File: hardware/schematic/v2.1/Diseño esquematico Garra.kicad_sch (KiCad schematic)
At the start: 20 parts

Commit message: fix: PDF
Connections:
- net SW renamed Stick_ON
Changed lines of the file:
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@@
 		)
 	)
-	(global_label "SW"
+	(global_label "Stick_ON"
 		(shape input)
 		(at 182.88 133.35 180)
@@
 		)
 	)
-	(global_label "SW"
+	(global_label "Stick_ON"
 		(shape input)
 		(at 269.24 143.51 0)

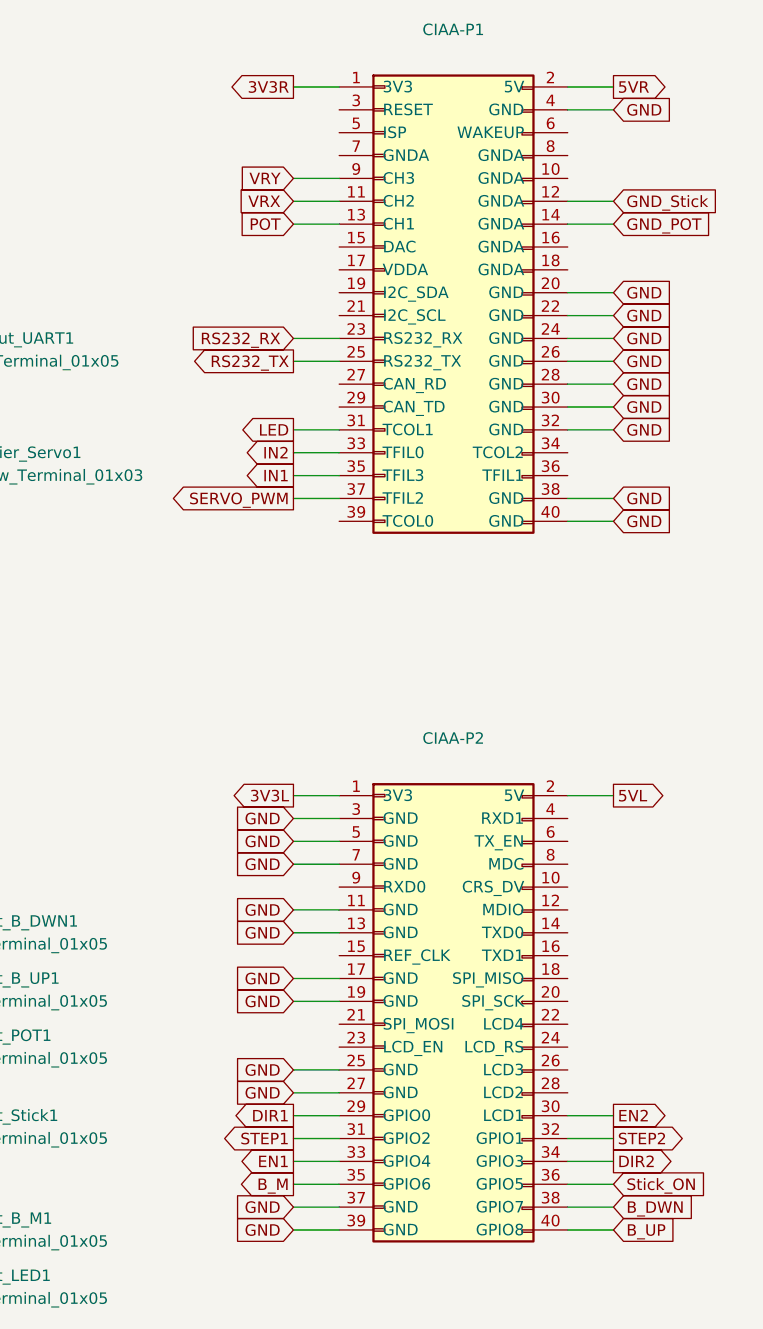
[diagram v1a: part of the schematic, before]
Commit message: Pcb branch (#8)
* refactor

* feat: PCB routing first stage completed

* docs: Schematics PDF added

* fix: PCB border colision

* feat: Copper layers added to the PCB

* feat: New PCB design with new components [LED, B_M]

* feat: add through holes for connectivity & GNDs links

* feat: hole diameter adjustment

* fix: PDF

* feat: change route system in PCB

---------

Co-authored-by: ManuSavenia <saveniamanuel@egmail.com>
Co-authored-by: Iván Valentín Polanis <polanis.ivan@alu.ing.unlp.edu.ar>
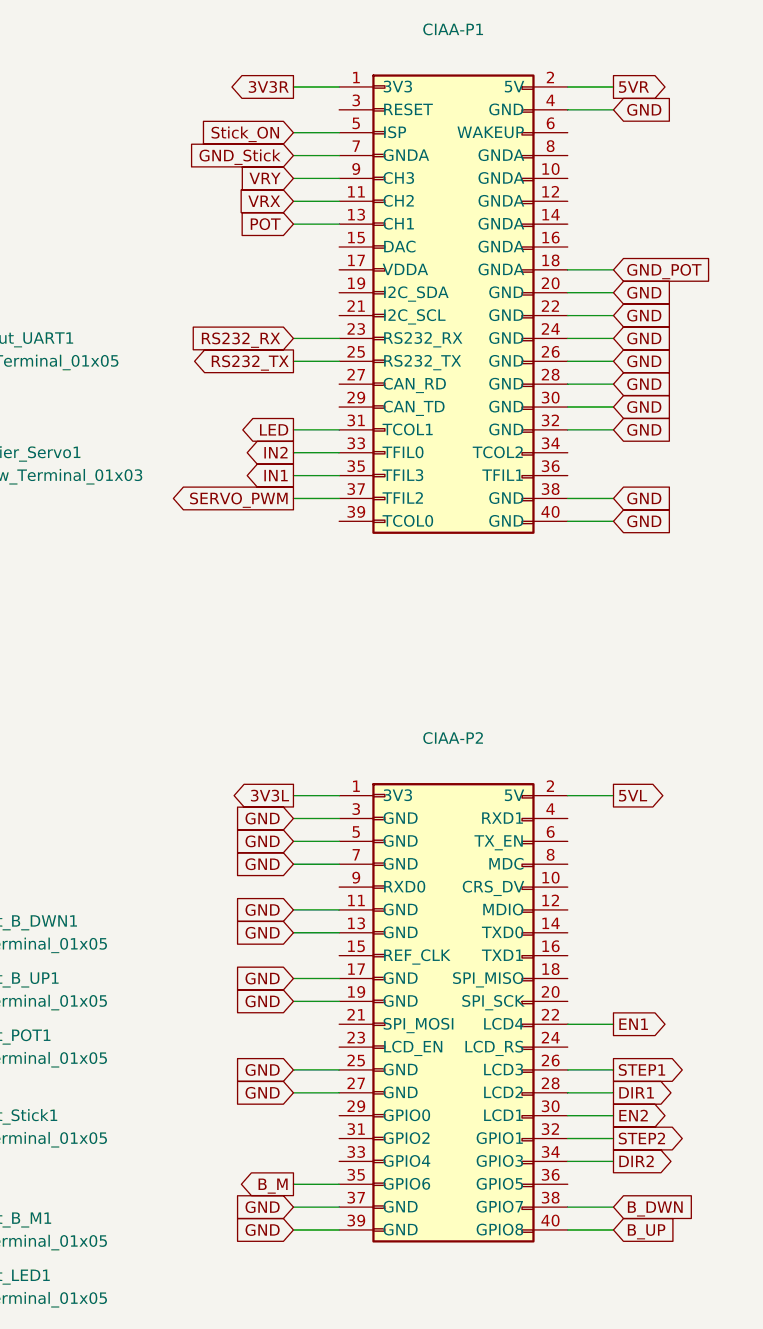
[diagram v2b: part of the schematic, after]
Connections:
- net DIR1: now also CIAA-P2.28 (LCD2); no longer CIAA-P2.29 (GPIO0)
- net EN1: now also CIAA-P2.22 (LCD4); no longer CIAA-P2.33 (GPIO4)
- net GND_POT: now also CIAA-P1.18 (GNDA); no longer CIAA-P1.14 (GNDA)
- net GND_Stick: now also CIAA-P1.7 (GNDA); no longer CIAA-P1.12 (GNDA)
- net STEP1: now also CIAA-P2.26 (LCD3); no longer CIAA-P2.31 (GPIO2)
- net Stick_ON: now also CIAA-P1.5 (ISP); no longer CIAA-P2.36 (GPIO5)
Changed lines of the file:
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@@
-	(wire
-		(pts
-			(xy 269.24 34.29) (xy 264.16 34.29)
-		)
-		(stroke
-			(width 0)
-			(type default)
-		)
-	)
 	(wire
 		(pts
@@
 	(wire
 		(pts
+			(xy 264.16 133.35) (xy 269.24 133.35)
+		)
+		(stroke
+			(width 0)
+			(type default)
+		)
+	)
+	(wire
+		(pts
 			(xy 189.23 85.09) (xy 189.23 86.36)
 		)
@@
 	(wire
 		(pts
-			(xy 233.68 135.89) (xy 238.76 135.89)
-		)
-		(stroke
-			(width 0)
-			(type default)
-		)
-	)
-	(wire
-		(pts
 			(xy 182.88 143.51) (xy 187.96 143.51)
 		)
@@
 	(wire
 		(pts
+			(xy 233.68 26.67) (xy 238.76 26.67)
+		)
+		(stroke
+			(width 0)
+			(type default)
+		)
+	)
+	(wire
+		(pts
 			(xy 71.12 86.36) (xy 80.01 86.36)
 		)
@@
 	(wire
 		(pts
-			(xy 233.68 138.43) (xy 238.76 138.43)
-		)
-		(stroke
-			(width 0)
-			(type default)
-		)
-	)
-	(wire
-		(pts
 			(xy 269.24 49.53) (xy 264.16 49.53)
 		)
@@
 	(wire
 		(pts
+			(xy 264.16 125.73) (xy 269.24 125.73)
+		)
+		(stroke
+			(width 0)
+			(type default)
+		)
+	)
+	(wire
+		(pts
 			(xy 184.15 66.04) (xy 189.23 66.04)
 		)
@@
 	(wire
 		(pts
-			(xy 269.24 36.83) (xy 264.16 36.83)
-		)
-		(stroke
-			(width 0)
-			(type default)
-		)
-	)
-	(wire
-		(pts
 			(xy 48.26 69.85) (xy 48.26 66.04)
 		)
@@
 	(wire
 		(pts
+			(xy 264.16 130.81) (xy 269.24 130.81)
+		)
+		(stroke
+			(width 0)
+			(type default)
+		)
+	)
+	(wire
+		(pts
 			(xy 182.88 149.86) (xy 187.96 149.86)
 		)
@@
 	(wire
 		(pts
+			(xy 264.16 41.91) (xy 269.24 41.91)
+		)
+		(stroke
+			(width 0)
+			(type default)
+		)
+	)
+	(wire
+		(pts
 			(xy 30.48 48.26) (xy 35.56 48.26)
 		)
@@
 	(wire
 		(pts
+			(xy 233.68 29.21) (xy 238.76 29.21)
+		)
+		(stroke
+			(width 0)
+			(type default)
+		)
+	)
+	(wire
+		(pts
 			(xy 72.39 64.77) (xy 74.93 64.77)
 		)
@@
 	(wire
 		(pts
-			(xy 264.16 143.51) (xy 269.24 143.51)
-		)
-		(stroke
-			(width 0)
-			(type default)
-		)
-	)
-	(wire
-		(pts
 			(xy 233.68 105.41) (xy 238.76 105.41)
 		)
@@
 		(pts
 			(xy 264.16 148.59) (xy 269.24 148.59)
-		)
-		(stroke
-			(width 0)
-			(type default)
-		)
-	)
-	(wire
-		(pts
-			(xy 233.68 140.97) (xy 238.76 140.97)
 		)
 		(stroke
@@
 	(global_label "DIR1"
 		(shape output)
-		(at 233.68 135.89 180)
-		(effects
-			(font
-				(size 1.27 1.27)
-			)
-			(justify right)
-		)
-		(property "Intersheetrefs" "${INTERSHEET_REFS}"
-			(at 233.68 135.89 0)
+		(at 269.24 133.35 0)
+		(effects
+			(font
+				(size 1.27 1.27)
+			)
+			(justify left)
+		)
+		(property "Intersheetrefs" "${INTERSHEET_REFS}"
+			(at 269.24 133.35 0)
 			(effects
 				(font
@@
 	(global_label "GND_POT"
 		(shape input)
-		(at 269.24 36.83 0)
-		(effects
-			(font
-				(size 1.27 1.27)
-			)
-			(justify left)
-		)
-		(property "Intersheetrefs" "${INTERSHEET_REFS}"
-			(at 269.24 36.83 0)
+		(at 269.24 41.91 0)
+		(effects
+			(font
+				(size 1.27 1.27)
+			)
+			(justify left)
+		)
+		(property "Intersheetrefs" "${INTERSHEET_REFS}"
+			(at 269.24 41.91 0)
 			(effects
 				(font
@@
 	(global_label "GND_Stick"
 		(shape input)
-		(at 269.24 34.29 0)
-		(effects
-			(font
-				(size 1.27 1.27)
-			)
-			(justify left)
-		)
-		(property "Intersheetrefs" "${INTERSHEET_REFS}"
-			(at 269.24 34.29 0)
-			(effects
-				(font
-					(size 1.27 1.27)
-				)
+		(at 233.68 29.21 180)
+		(effects
+			(font
+				(size 1.27 1.27)
+			)
+			(justify right)
+		)
+		(property "Intersheetrefs" "${INTERSHEET_REFS}"
+			(at 233.68 29.21 0)
+			(effects
+				(font
+					(size 1.27 1.27)
+				)
+				(justify left)
 				(hide yes)
 			)
@@
 					(size 1.27 1.27)
 				)
-				(hide yes)
-			)
-		)
-	)
-	(global_label "Stick_ON"
-		(shape input)
-		(at 269.24 143.51 0)
-		(effects
-			(font
-				(size 1.27 1.27)
-			)
-			(justify left)
-		)
-		(property "Intersheetrefs" "${INTERSHEET_REFS}"
-			(at 269.24 143.51 0)
-			(effects
-				(font
-					(size 1.27 1.27)
-				)
-				(justify left)
 				(hide yes)
 			)
@@
 	(global_label "EN1"
 		(shape output)
-		(at 233.68 140.97 180)
-		(effects
-			(font
-				(size 1.27 1.27)
-			)
-			(justify right)
-		)
-		(property "Intersheetrefs" "${INTERSHEET_REFS}"
-			(at 233.68 140.97 0)
+		(at 269.24 125.73 0)
+		(effects
+			(font
+				(size 1.27 1.27)
+			)
+			(justify left)
+		)
+		(property "Intersheetrefs" "${INTERSHEET_REFS}"
+			(at 269.24 125.73 0)
 			(effects
 				(font
@@
 	(global_label "STEP1"
 		(shape output)
-		(at 233.68 138.43 180)
-		(effects
-			(font
-				(size 1.27 1.27)
-			)
-			(justify right)
-		)
-		(property "Intersheetrefs" "${INTERSHEET_REFS}"
-			(at 233.68 138.43 0)
+		(at 269.24 130.81 0)
+		(effects
+			(font
+				(size 1.27 1.27)
+			)
+			(justify left)
+		)
+		(property "Intersheetrefs" "${INTERSHEET_REFS}"
+			(at 269.24 130.81 0)
 			(effects
 				(font
@@
 			(effects
 				(font
+					(size 1.27 1.27)
+				)
+				(justify right)
+				(hide yes)
+			)
+		)
+	)
+	(global_label "Stick_ON"
+		(shape input)
+		(at 233.68 26.67 180)
+		(effects
+			(font
+				(size 1.27 1.27)
+			)
+			(justify right)
+		)
+		(property "Intersheetrefs" "${INTERSHEET_REFS}"
+			(at 233.68 26.67 0)
+			(effects
+				(font

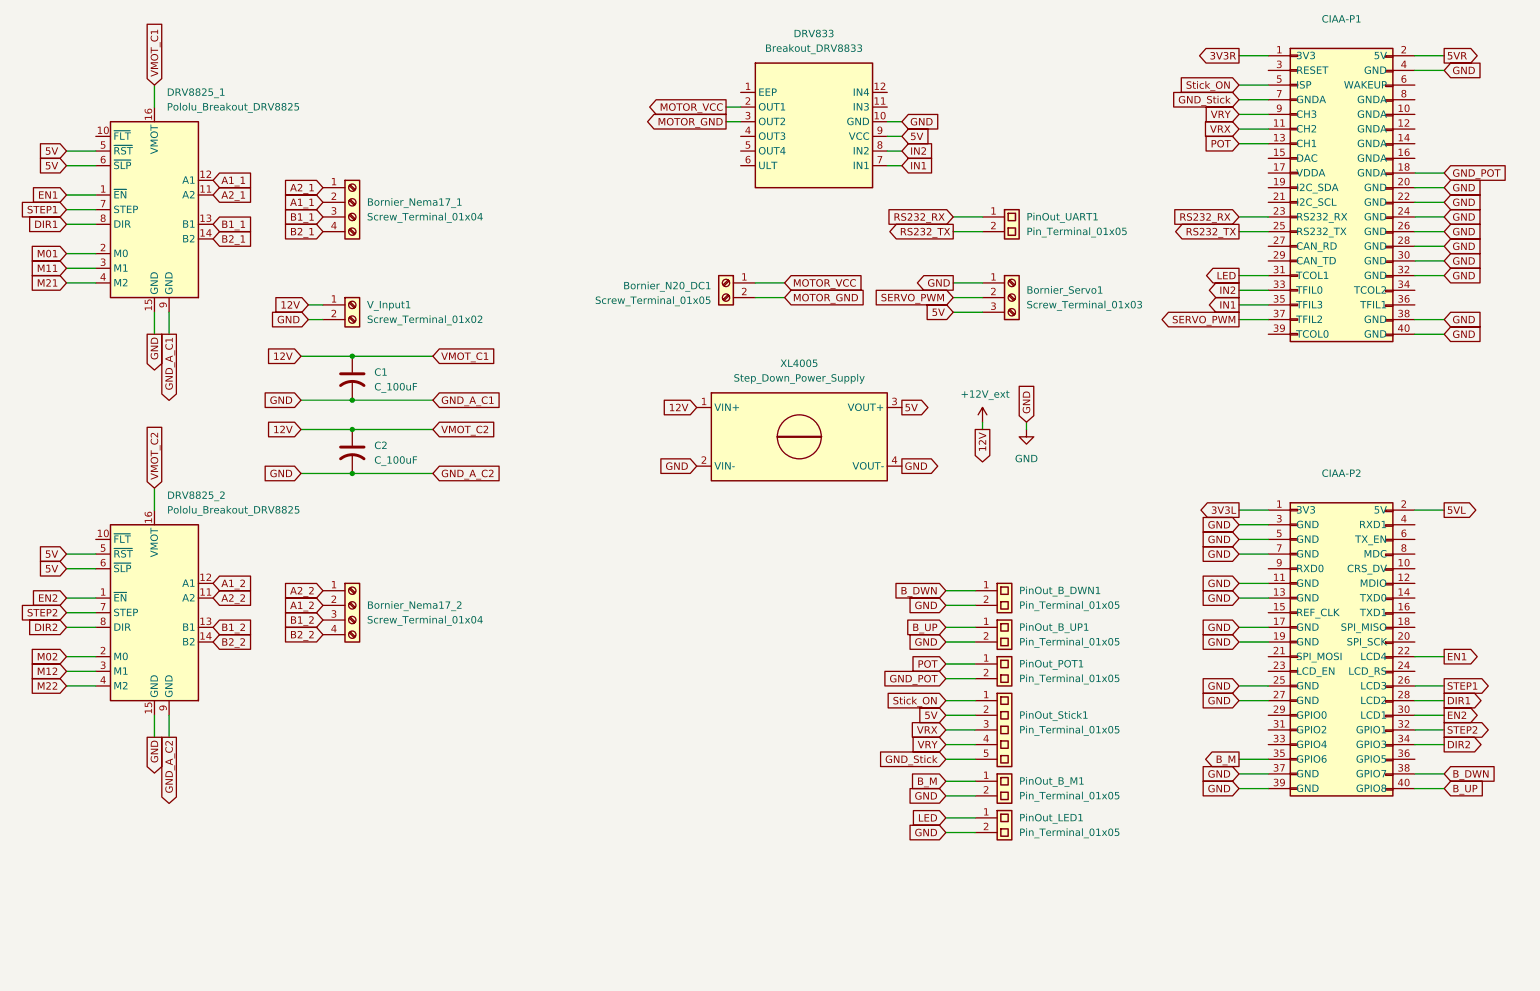
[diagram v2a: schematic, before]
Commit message: feat: add new esp32 schematic
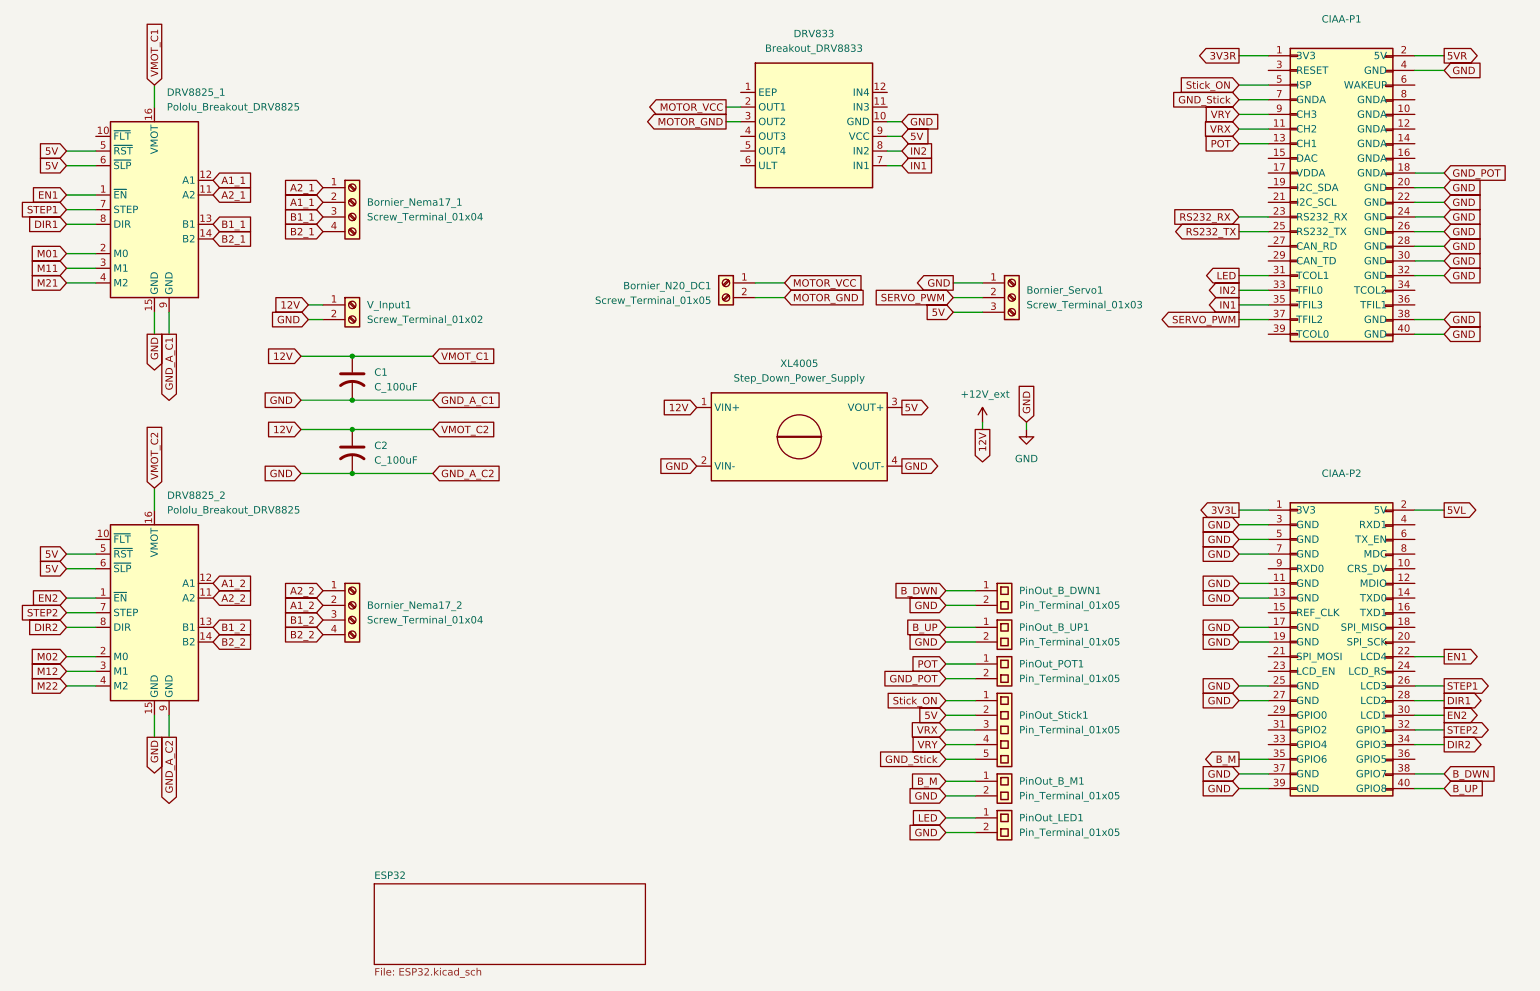
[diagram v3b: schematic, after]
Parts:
- removed PinOut_UART1: Pin_Terminal_01x05, Connector_PinSocket_2.00mm:PinSocket_1x02_P2.00mm_Vertical, symbol Connector:Screw_Terminal_01x02
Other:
- added sheet ESP32 (ESP32.kicad_sch)
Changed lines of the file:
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@@
 	(wire
 		(pts
-			(xy 184.15 49.53) (xy 189.23 49.53)
-		)
-		(stroke
-			(width 0)
-			(type default)
-		)
-	)
-	(wire
-		(pts
 			(xy 30.48 45.72) (xy 35.56 45.72)
 		)
@@
 	(wire
 		(pts
-			(xy 184.15 52.07) (xy 189.23 52.07)
-		)
-		(stroke
-			(width 0)
-			(type default)
-		)
-	)
-	(wire
-		(pts
 			(xy 30.48 125.73) (xy 35.56 125.73)
 		)
@@
 		)
 	)
-	(global_label "RS232_TX"
-		(shape output)
-		(at 184.15 52.07 180)
-		(effects
-			(font
-				(size 1.27 1.27)
-			)
-			(justify right)
-		)
-		(property "Intersheetrefs" "${INTERSHEET_REFS}"
-			(at 184.15 52.07 0)
-			(effects
-				(font
-					(size 1.27 1.27)
-				)
-				(hide yes)
-			)
-		)
-	)
 	(global_label "GND"
 		(shape input)
@@
 		)
 	)
-	(global_label "RS232_RX"
-		(shape input)
-		(at 184.15 49.53 180)
-		(effects
-			(font
-				(size 1.27 1.27)
-			)
-			(justify right)
-		)
-		(property "Intersheetrefs" "${INTERSHEET_REFS}"
-			(at 184.15 49.53 0)
-			(effects
-				(font
-					(size 1.27 1.27)
-				)
-				(hide yes)
-			)
-		)
-	)
 	(global_label "GND"
 		(shape output)
@@
 	)
 	(symbol
-		(lib_name "Screw_Terminal_01x02_3")
-		(lib_id "Connector:Screw_Terminal_01x02")
-		(at 194.31 49.53 0)
-		(unit 1)
-		(exclude_from_sim no)
-		(in_bom yes)
-		(on_board yes)
-		(dnp no)
-		(fields_autoplaced yes)
-		(property "Reference" "PinOut_UART1"
-			(at 196.85 49.5299 0)
-			(effects
-				(font
-					(size 1.27 1.27)
-				)
-				(justify left)
-			)
-		)
-		(property "Value" "Pin_Terminal_01x05"
-			(at 196.85 52.0699 0)
-			(effects
-				(font
-					(size 1.27 1.27)
-				)
-				(justify left)
-			)
-		)
-		(property "Footprint" "Connector_PinSocket_2.00mm:PinSocket_1x02_P2.00mm_Vertical"
-			(at 194.564 44.196 0)
-			(effects
-				(font
-					(size 1.27 1.27)
-				)
-				(hide yes)
-			)
-		)
-		(property "Datasheet" "~"
-			(at 195.834 54.102 0)
-			(effects
-				(font
-					(size 1.27 1.27)
-				)
-				(hide yes)
-			)
-		)
-		(property "Description" "Generic screw terminal, single row, 01x02, script generated (kicad-library-utils/schlib/autogen/connector/)"
-			(at 194.818 55.118 0)
-			(effects
-				(font
-					(size 1.27 1.27)
-				)
-				(hide yes)
-			)
-		)
-		(pin "2"
-		)
-		(pin "1"
-		)
-		(instances
-			(project "Diseño esquematico Garra"
-				(path "/a88248f6-7b70-4a9d-b538-4e8e42a3a066"
-					(reference "PinOut_UART1")
-					(unit 1)
-				)
-			)
-		)
-	)
-	(symbol
 		(lib_id "Connector:Screw_Terminal_01x02")
 		(at 80.01 64.77 0)
@@
 				)
 			)
+		)
+	)
+	(sheet
+		(at 83.82 165.1)
+		(size 46.99 13.97)
+		(exclude_from_sim no)
+		(in_bom yes)
+		(on_board yes)
+		(dnp no)
+		(fields_autoplaced yes)
+		(stroke
+			(width 0.1524)
+			(type solid)
+		)
+		(fill
+			(color 0 0 0 0.0000)
+		)
+		(property "Sheetname" "ESP32"
+			(at 83.82 164.3884 0)
+			(effects
+				(font
+					(size 1.27 1.27)
+				)
+				(justify left bottom)
+			)
+		)
+		(property "Sheetfile" "ESP32.kicad_sch"
+			(at 83.82 179.6546 0)
+			(effects
+				(font
+					(size 1.27 1.27)
+				)
+				(justify left top)
+			)
+		)
+		(instances
+			(project "Diseño esquematico Garra"
+				(path "/a88248f6-7b70-4a9d-b538-4e8e42a3a066"
+					(page "2")
+				)
+			)

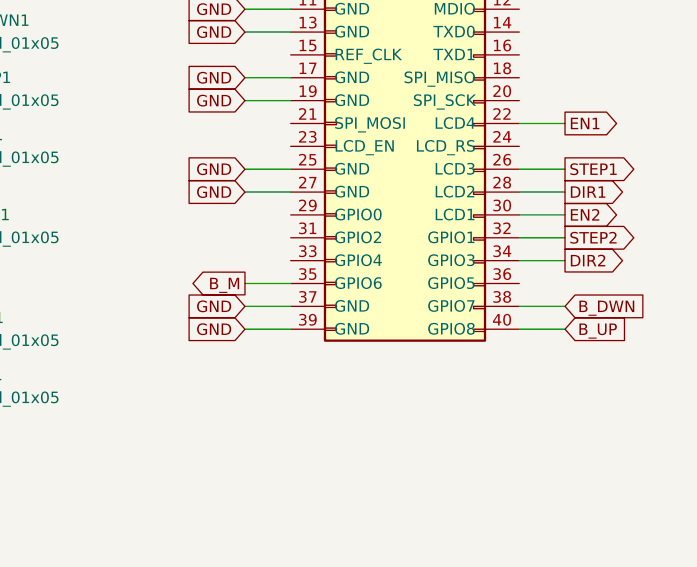
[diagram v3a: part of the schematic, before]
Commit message: feat: take png and pdf from finished schematic
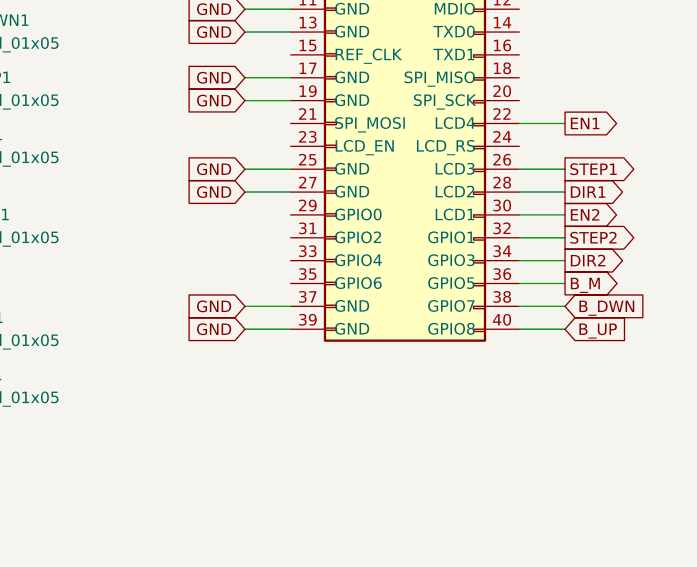
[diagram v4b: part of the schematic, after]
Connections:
- net B_M: now also CIAA-P2.36 (GPIO5); no longer CIAA-P2.35 (GPIO6)
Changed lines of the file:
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@@
+	(wire
+		(pts
+			(xy 264.16 143.51) (xy 269.24 143.51)
+		)
+		(stroke
+			(width 0)
+			(type default)
+		)
+	)
 	(wire
 		(pts
@@
 		(pts
 			(xy 233.68 115.57) (xy 238.76 115.57)
-		)
-		(stroke
-			(width 0)
-			(type default)
-		)
-	)
-	(wire
-		(pts
-			(xy 233.68 143.51) (xy 238.76 143.51)
 		)
 		(stroke
@@
 	(global_label "B_M"
 		(shape output)
-		(at 233.68 143.51 180)
-		(effects
-			(font
-				(size 1.27 1.27)
-			)
-			(justify right)
-		)
-		(property "Intersheetrefs" "${INTERSHEET_REFS}"
-			(at 233.68 143.51 0)
-			(effects
-				(font
+		(at 269.24 143.51 0)
+		(effects
+			(font
+				(size 1.27 1.27)
+			)
+			(justify left)
+		)
+		(property "Intersheetrefs" "${INTERSHEET_REFS}"
+			(at 269.24 143.51 0)
+			(effects
+				(font
